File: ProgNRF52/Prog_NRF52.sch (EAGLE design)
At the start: 48 parts, among them J3 MEC1-108-02-XX-D-A, U1 TS5A9411, U2 SN74LVC1GU04DBV, U3 TS5A9411, U4 TS5A9411, U5 SN74LVC1GU04DBV, U6 TXB0102D

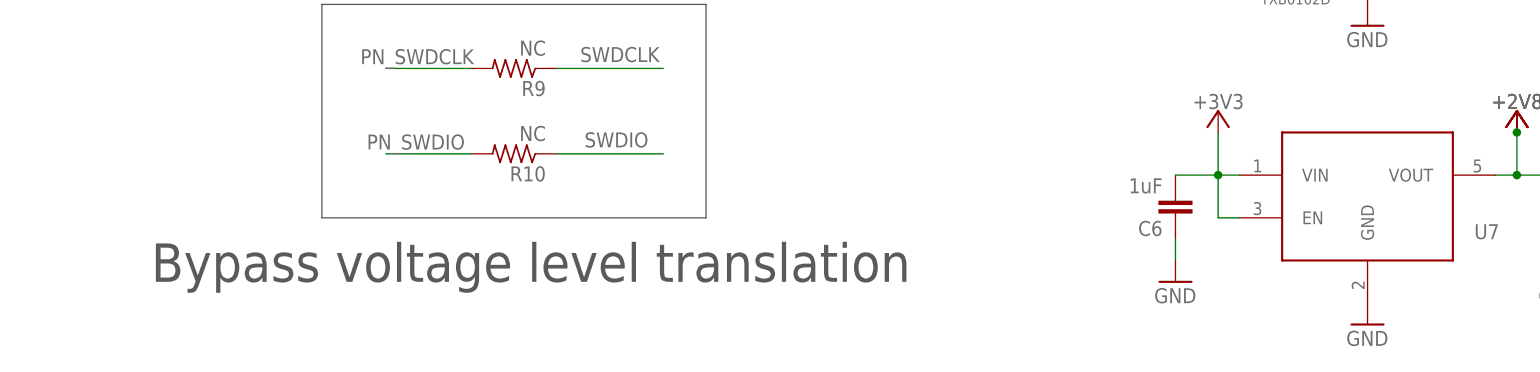
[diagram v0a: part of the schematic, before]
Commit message: Test specific modif
Changing bom and comments
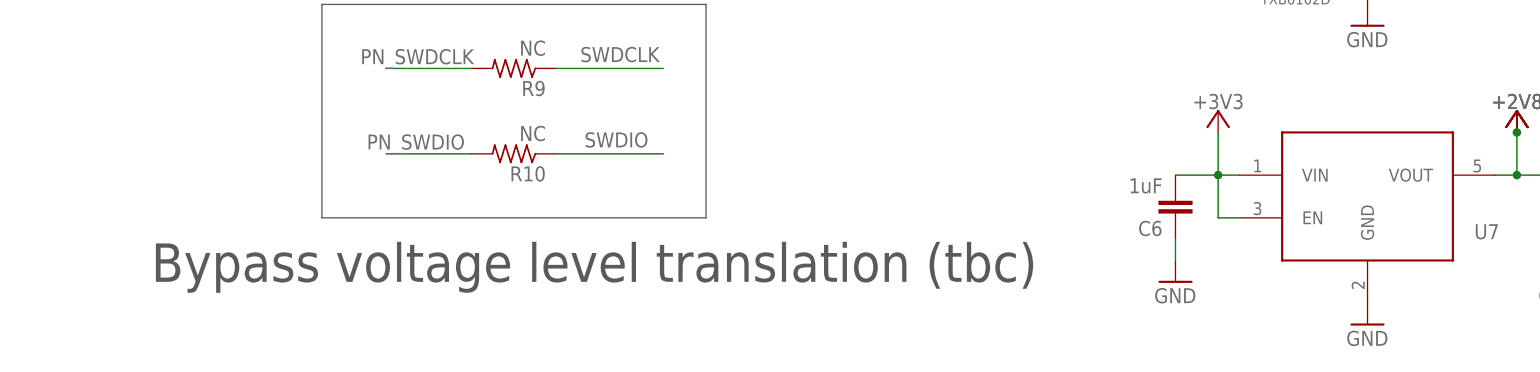
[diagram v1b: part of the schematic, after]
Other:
- note added: "Bypass voltage level translation (tbc)"
- note removed: "Bypass voltage level translation"
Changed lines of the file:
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@@
 <wire x1="132.08" y1="38.1" x2="132.08" y2="63.5" width="0.1524" layer="97"/>
 <wire x1="132.08" y1="63.5" x2="86.36" y2="63.5" width="0.1524" layer="97"/>
-<text x="66.04" y="30.48" size="4.572" layer="97">Bypass voltage level translation</text>
+<text x="66.04" y="30.48" size="4.572" layer="97">Bypass voltage level translation (tbc)</text>
 </plain>
 <instances>

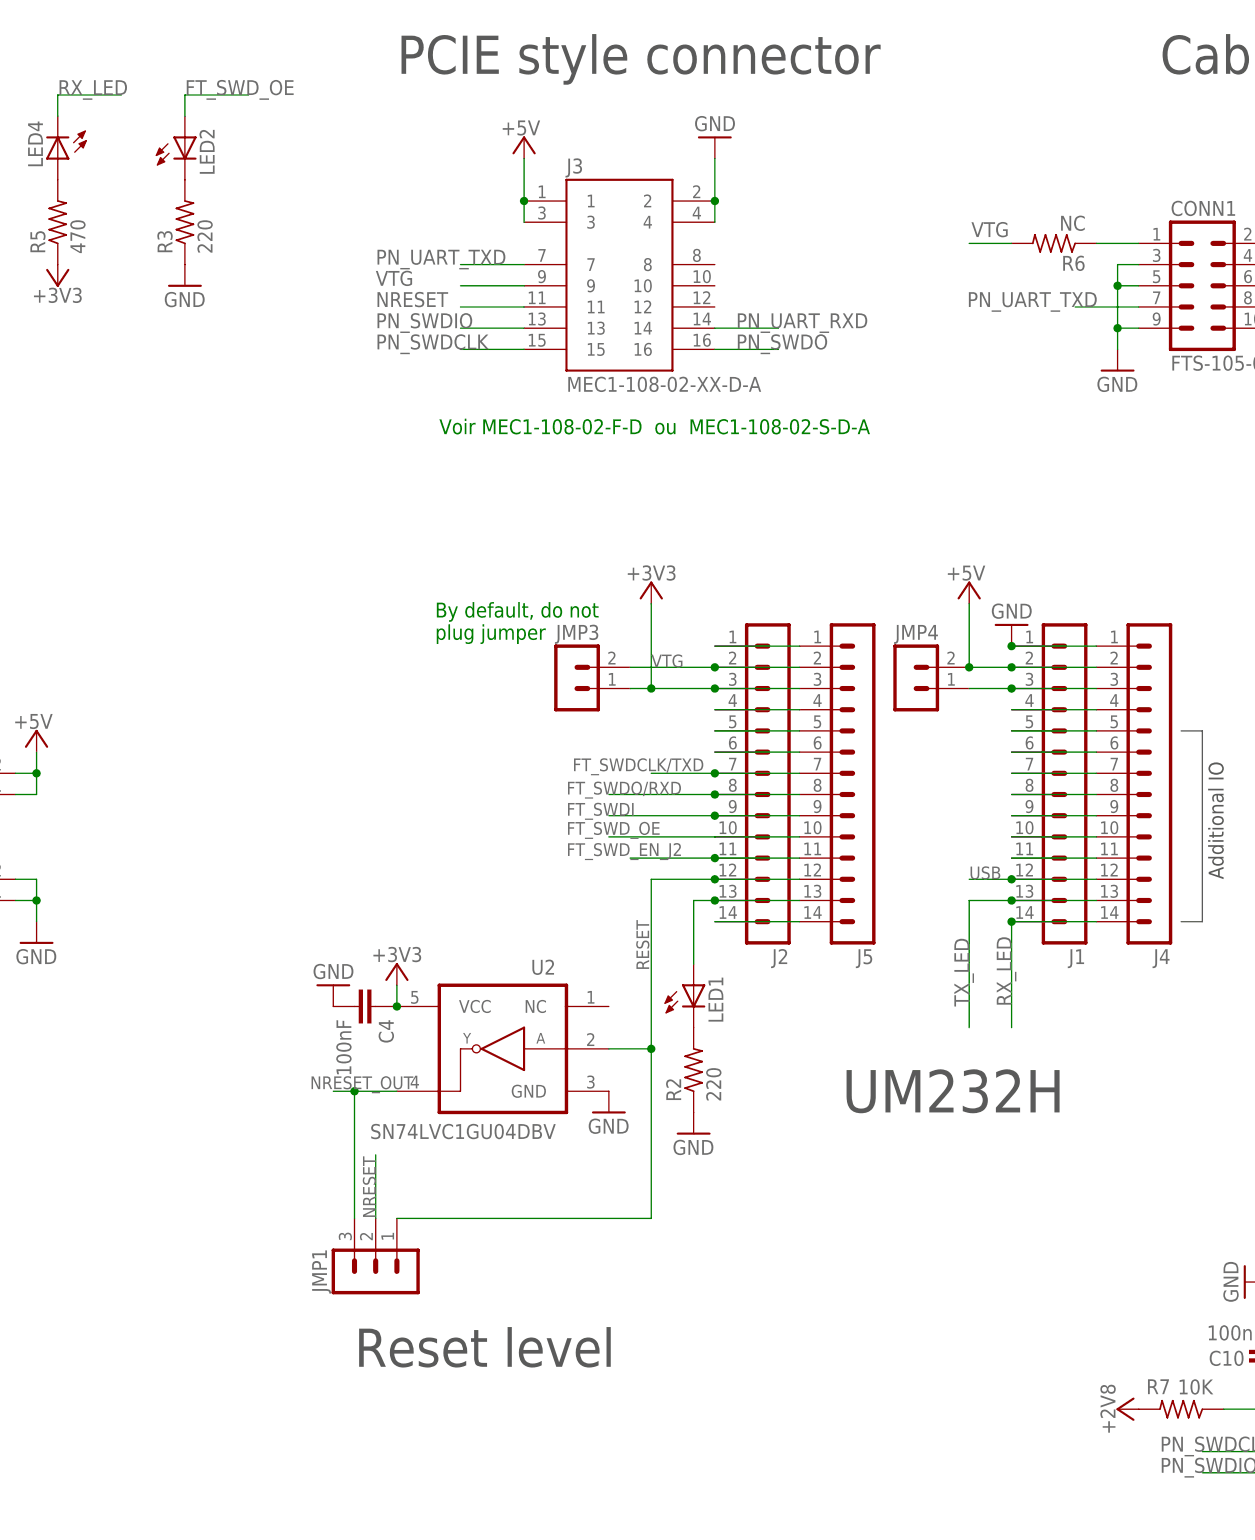
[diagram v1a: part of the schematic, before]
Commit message: update schematic comments
update schematic and layout
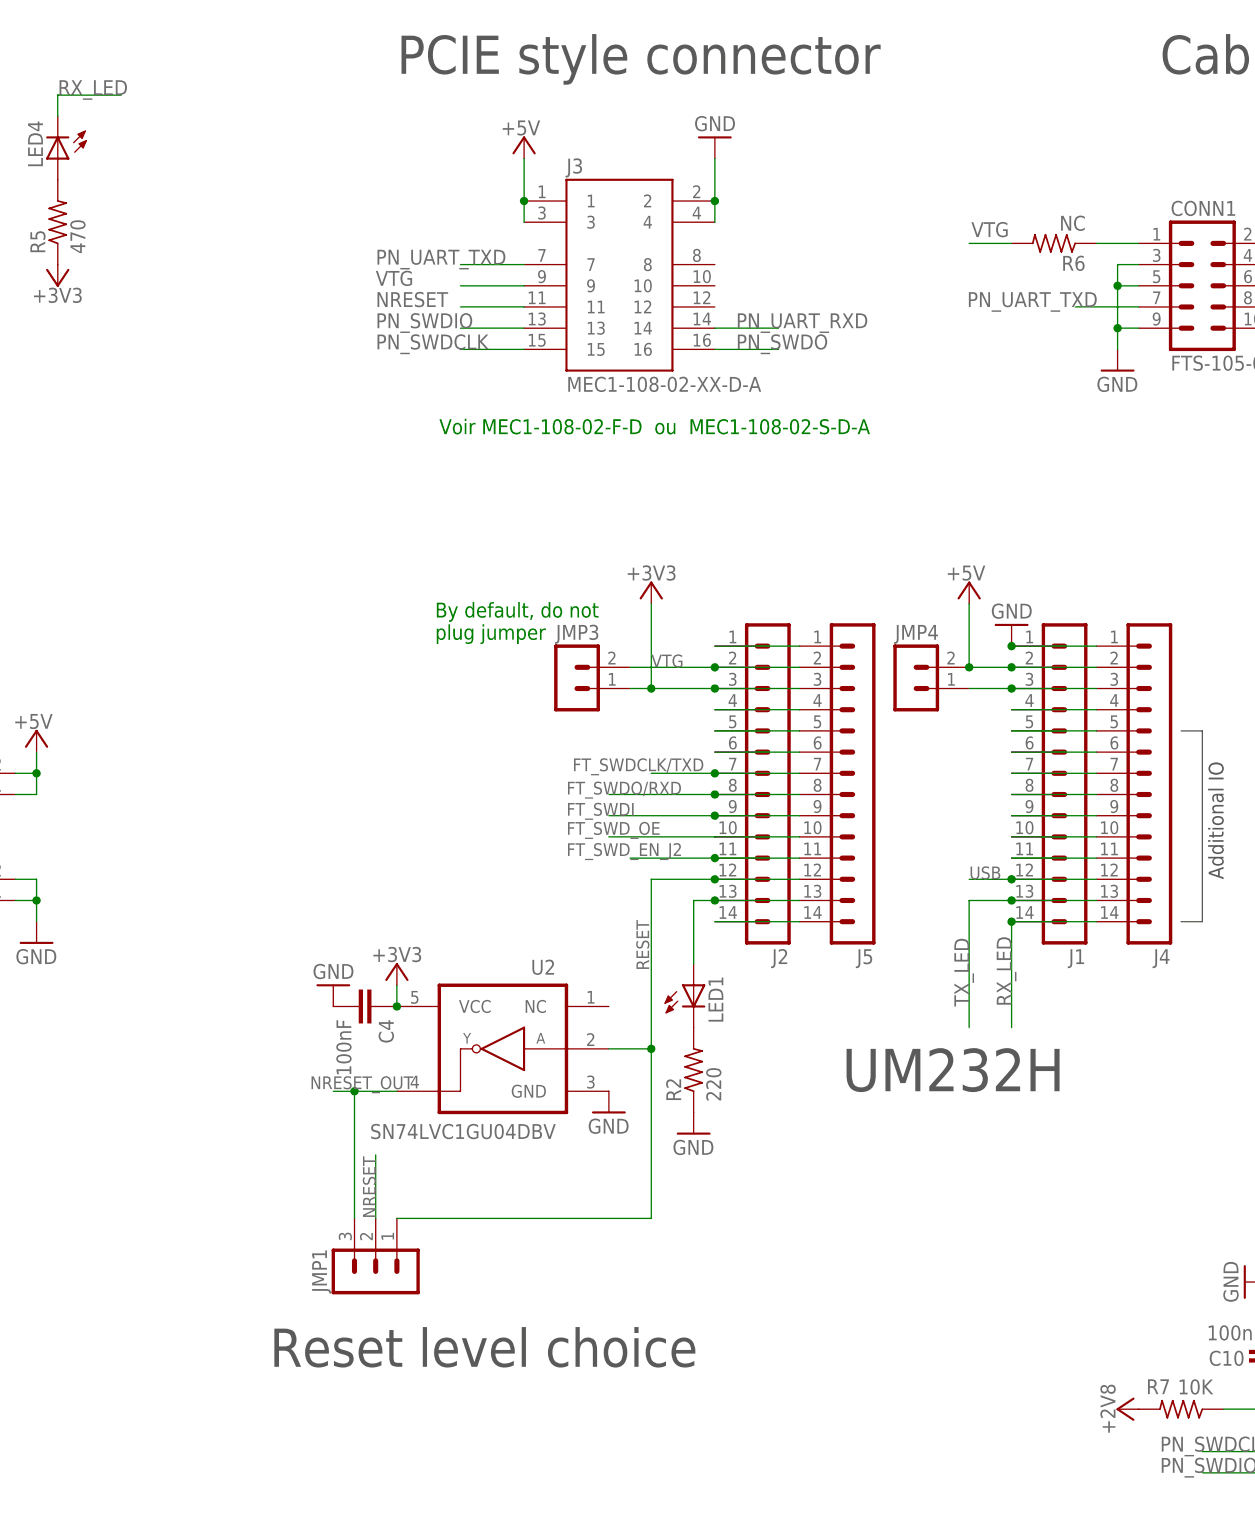
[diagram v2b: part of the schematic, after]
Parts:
- removed LED2: (no value), led:LEDCHIP-LED0603
- removed R3: 220, resistor:R-US_R0603
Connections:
- removed net N$4: LED2.C, R3.2
- net FT_SWD_OE: no longer LED2.A
- net GND: no longer R3.1
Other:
- note added: "Reset level choice"
- note removed: "Reset level"
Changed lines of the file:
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@@
 <part name="JMP2" library="con-lstb" deviceset="MA03-1" device=""/>
 <part name="JMP1" library="con-lstb" deviceset="MA03-1" device=""/>
-<part name="LED2" library="led" deviceset="LED" device="CHIP-LED0603"/>
-<part name="R3" library="resistor" deviceset="R-US_" device="R0603" value="220"/>
-<part name="GND6" library="supply1" deviceset="GND" device=""/>
 <part name="J3" library="TestBench_MUX" deviceset="MEC1-108-02-XX-D-A" device=""/>
 <part name="J6" library="con-lstb" deviceset="MA02-1" device=""/>
@@
 <plain>
 <text x="180.34" y="243.84" size="4.572" layer="97">Cable</text>
-<text x="142.24" y="119.38" size="5.08" layer="97">UM232H</text>
+<text x="142.24" y="121.92" size="5.08" layer="97">UM232H</text>
 <wire x1="182.88" y1="142.24" x2="185.42" y2="142.24" width="0.1524" layer="97"/>
 <wire x1="185.42" y1="142.24" x2="185.42" y2="165.1" width="0.1524" layer="97"/>
@@
 <text x="93.472" y="176.022" size="1.778" layer="91">By default, do not
 plug jumper</text>
-<text x="83.82" y="88.9" size="4.572" layer="97">Reset level</text>
+<text x="73.66" y="88.9" size="4.572" layer="97">Reset level choice</text>
 <text x="93.98" y="200.66" size="1.778" layer="91">Voir MEC1-108-02-F-D  ou  MEC1-108-02-S-D-A</text>
 <text x="88.9" y="243.84" size="4.572" layer="97">PCIE style connector</text>
@@
 <instance part="JMP2" gate="G$1" x="335.28" y="134.62" rot="R180"/>
 <instance part="JMP1" gate="G$1" x="86.36" y="99.06" rot="R90"/>
-<instance part="LED2" gate="G$1" x="63.5" y="236.22"/>
-<instance part="R3" gate="G$1" x="63.5" y="226.06" rot="R90"/>
-<instance part="GND6" gate="1" x="63.5" y="218.44"/>
 <instance part="J3" gate="G$1" x="104.14" y="228.6"/>
 <instance part="J6" gate="G$1" x="35.56" y="160.02"/>
@@
 </segment>
 <segment>
-<pinref part="R3" gate="G$1" pin="1"/>
-<pinref part="GND6" gate="1" pin="GND"/>
-</segment>
-<segment>
 <pinref part="J7" gate="G$1" pin="1"/>
 <pinref part="GND14" gate="1" pin="GND"/>
@@
 </segment>
 </net>
-<net name="N$4" class="0">
-<segment>
-<pinref part="LED2" gate="G$1" pin="C"/>
-<pinref part="R3" gate="G$1" pin="2"/>
-</segment>
-</net>
 <net name="SWDO/RXD_1" class="0">
 <segment>
@@
 <label x="274.32" y="99.06" size="1.778" layer="95"/>
 </segment>
-<segment>
-<pinref part="LED2" gate="G$1" pin="A"/>
-<wire x1="63.5" y1="238.76" x2="63.5" y2="241.3" width="0.1524" layer="91"/>
-<wire x1="63.5" y1="241.3" x2="71.12" y2="241.3" width="0.1524" layer="91"/>
-<label x="63.5" y="241.3" size="1.778" layer="95"/>
-</segment>
-</net>
+</net>

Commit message: Suppress led on schematic
Useless led where suppress
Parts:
- removed LED4: (no value), led:LEDCHIP-LED0603
- removed R5: 470, resistor:R-US_R0603
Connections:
- removed net N$7: LED4.A, R5.2
- net +3V3: no longer R5.1
- net RX_LED: no longer LED4.C
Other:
- moved on the sheet: C10, C2, C3, C8, C9, JMP2, R1, R7, U1, U4, U6
